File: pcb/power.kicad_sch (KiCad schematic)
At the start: 59 parts, among them J7 1S LiPo, Q1 Q_Dual_NMOS_S1G1S2G2D2D2D1D1, Q2 Q_Dual_NMOS_S1G1S2G2D2D2D1D1, U13 BQ25798, U14 TPS63060, U15 TPS61089

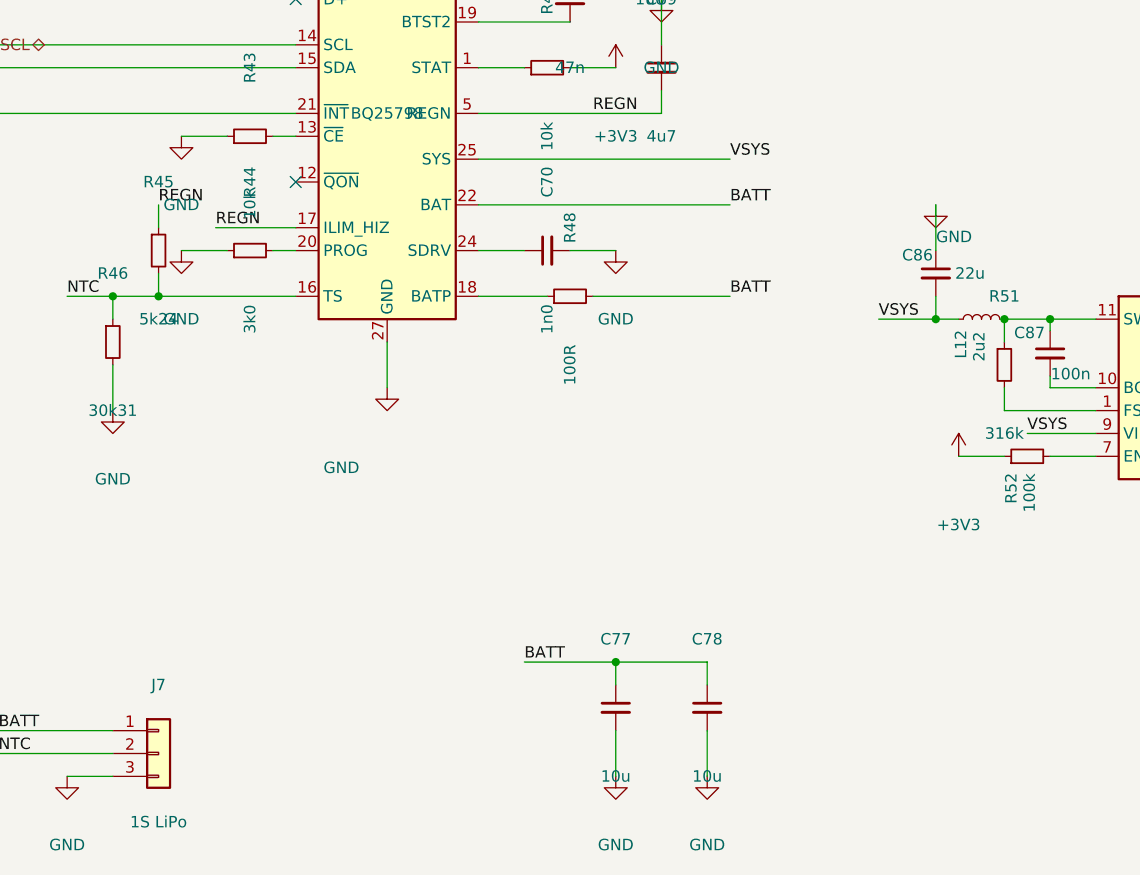
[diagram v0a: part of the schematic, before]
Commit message: give the battery a switch, so the board has an off
Patched into the power sheet the same way as the input pairs: named removals by coordinate, the new
work appended, nothing hand-placed moved.

The reason is in the schematic rather than in a datasheet. The 3.3V converter has its enable tied
straight to the system rail and the 5V converter's is pulled up to the 3.3V rail, so neither is
under firmware control, so for as long as the cell is connected the processor, the flash, the hub
and the port rail are all live and the deepest state firmware can reach is sleep. This switch is
the only thing on the board that disconnects the battery.

The argument is not that the charger leaks: its battery-only draw is 17uA, which on this cell is
measured in years. It is that everything else stays powered, and against that the charger's
shutdown state is 500nA. The size of that gap is the point. The figure on the other side of it is
an estimate of a sleeping-but-powered board and wants measuring rather than believing.

Wake is safe, which is the objection that would otherwise sink it: both low-power states wake
unconditionally on a charger being plugged in, and ship mode also by register or by the reset
input. No sequence strands the device.

The part is the one already in the design for the input pairs, both halves in parallel -- about
10 milliohms, so 35mV and 0.12W at the 3.5A peak and 18mV at the declared budget, and 30nC against
a 100nA charge pump at half duty is roughly 600ms to close, which is nothing for a power path.

Two consequences are easy to miss and both are taken. The capacitor that the driver pin wants when
no switch is fitted comes out, because against 100nA it would only add delay. And the battery sense
resistor stays on the cell side, so the charger can still see the battery while the switch is open
-- the same discipline that puts each input's detect pin outside its own pair. The drains face the
cell so the body diodes block pack-to-system when the switch is ope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
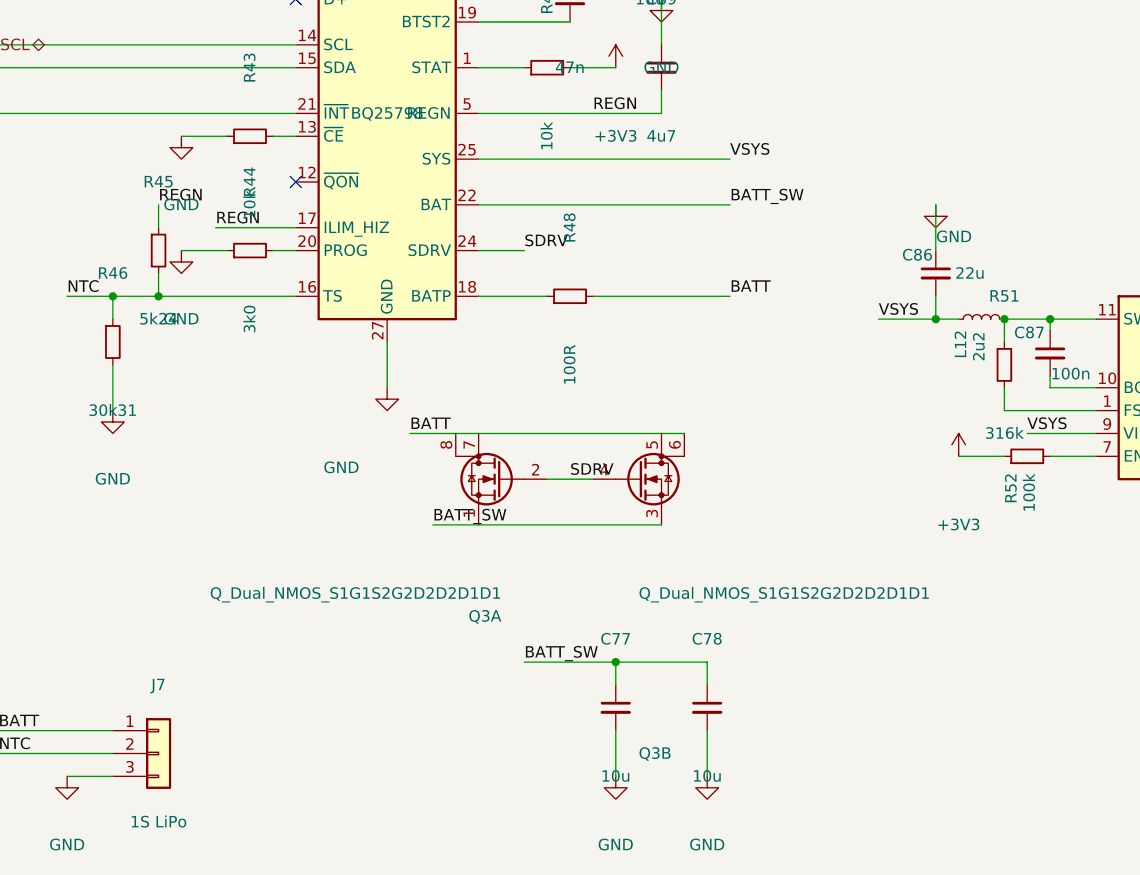
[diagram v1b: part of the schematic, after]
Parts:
- removed C70: 1n0, symbol Device:C_Small
- added Q3: Q_Dual_NMOS_S1G1S2G2D2D2D1D1, symbol Transistor_FET:Q_Dual_NMOS_S1G1S2G2D2D2D1D1
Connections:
- net BATT: now also Q3.5 (D), Q3.6 (D), Q3.7 (D), Q3.8 (D); no longer C77.1, C78.1, U13.22 (BAT), U13.23 (BAT)
- net SDRV: now reaches U13.24 (SDRV)
- net SDRV: now also Q3.2 (G), Q3.4 (G)
- new net BATT_SW: C77.1, C78.1, Q3.1 (S), Q3.3 (S), U13.22 (BAT), U13.23 (BAT)
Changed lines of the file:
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@@
 	(wire
 		(pts
-			(xy 198.12 149.86) (xy 203.2 149.86)
-		)
-		(stroke
-			(width 0)
-			(type solid)
-		)
-	)
-	(wire
-		(pts
 			(xy 109.22 82.55) (xy 118.11 82.55)
 		)
@@
 		)
 	)
-	(label "BATT"
+	(label "BATT_SW"
 		(at 193.04 195.58 0)
 		(effects
@@
 		)
 	)
-	(label "BATT"
+	(label "BATT_SW"
 		(at 215.9 144.78 0)
 		(effects
@@
 	)
 	(symbol
-		(lib_id "power:GND")
-		(at 203.2 149.86 0)
-		(unit 1)
-		(body_style 1)
-		(exclude_from_sim no)
-		(in_bom yes)
-		(on_board yes)
-		(in_pos_files yes)
-		(dnp no)
-		(property "Reference" "#PWR01"
-			(at 203.2 142.24 0)
-			(hide yes)
-			(show_name no)
-			(do_not_autoplace no)
-			(effects
-				(font
-					(size 1.27 1.27)
-				)
-			)
-		)
-		(property "Value" "GND"
-			(at 203.2 157.48 0)
-			(show_name no)
-			(do_not_autoplace no)
-			(effects
-				(font
-					(size 1.27 1.27)
-				)
-			)
-		)
-		(property "Footprint" ""
-			(at 203.2 149.86 0)
-			(show_name no)
-			(do_not_autoplace no)
-			(effects
-				(font
-					(size 1.27 1.27)
-				)
-			)
-		)
-		(property "Datasheet" ""
-			(at 203.2 149.86 0)
-			(show_name no)
-			(do_not_autoplace no)
-			(effects
-				(font
-					(size 1.27 1.27)
-				)
-			)
-		)
-		(property "Description" ""
-			(at 203.2 149.86 0)
-			(show_name no)
-			(do_not_autoplace no)
-			(effects
-				(font
-					(size 1.27 1.27)
-				)
-			)
-		)
-		(pin "1"
-		)
-		(instances
-			(project "crossfire"
-				(path "/4c5cdd13-4f54-43b0-affb-0ae4b9a4d279/3a0d800d-f868-47e5-a520-4703480651cc"
-					(reference "#PWR01")
-					(unit 1)
-				)
-			)
-		)
-	)
-	(symbol
 		(lib_id "Device:R_Small")
 		(at 246.38 162.56 0)
@@
 	)
 	(symbol
-		(lib_id "Device:C_Small")
-		(at 195.58 149.86 90)
-		(unit 1)
-		(body_style 1)
-		(exclude_from_sim no)
-		(in_bom yes)
-		(on_board yes)
-		(in_pos_files yes)
-		(dnp no)
-		(property "Reference" "C70"
-			(at 195.58 142.24 0)
-			(show_name no)
-			(do_not_autoplace no)
-			(effects
-				(font
-					(size 1.27 1.27)
-				)
-			)
-		)
-		(property "Value" "1n0"
-			(at 195.58 157.48 0)
-			(show_name no)
-			(do_not_autoplace no)
-			(effects
-				(font
-					(size 1.27 1.27)
-				)
-			)
-		)
-		(property "Footprint" ""
-			(at 195.58 149.86 0)
-			(show_name no)
-			(do_not_autoplace no)
-			(effects
-				(font
-					(size 1.27 1.27)
-				)
-			)
-		)
-		(property "Datasheet" ""
-			(at 195.58 149.86 0)
-			(show_name no)
-			(do_not_autoplace no)
-			(effects
-				(font
-					(size 1.27 1.27)
-				)
-			)
-		)
-		(property "Description" ""
-			(at 195.58 149.86 0)
-			(show_name no)
-			(do_not_autoplace no)
-			(effects
-				(font
-					(size 1.27 1.27)
-				)
-			)
-		)
-		(pin "1"
-		)
-		(pin "2"
-		)
-		(instances
-			(project "crossfire"
-				(path "/4c5cdd13-4f54-43b0-affb-0ae4b9a4d279/3a0d800d-f868-47e5-a520-4703480651cc"
-					(reference "C70")
-					(unit 1)
-				)
-			)
-		)
-	)
-	(symbol
 		(lib_id "power:+3V3")
 		(at 119.38 114.3 0)
@@
 		)
 	)
+	(symbol
+		(lib_id "Transistor_FET:Q_Dual_NMOS_S1G1S2G2D2D2D1D1")
+		(at 190.50 175.26 0)
+		(mirror y)
+		(unit 1)
+		(body_style 1)
+		(exclude_from_sim no)
+		(in_bom yes)
+		(on_board yes)
+		(in_pos_files yes)
+		(dnp no)
+		(property "Reference" "Q3"
+			(at 190.50 190.50 0)
+			(show_name no)
+			(do_not_autoplace no)
+			(effects
+				(font
+					(size 1.27 1.27)
+				)
+				(justify left)
+			)
+		)
+		(property "Value" "Q_Dual_NMOS_S1G1S2G2D2D2D1D1"
+			(at 190.50 187.96 0)
+			(show_name no)
+			(do_not_autoplace no)
+			(effects
+				(font
+					(size 1.27 1.27)
+				)
+				(justify left)
+			)
+		)
+		(property "Footprint" ""
+			(at 190.50 175.26 0)
+			(show_name no)
+			(do_not_autoplace no)
+			(effects
+				(font
+					(size 1.27 1.27)
+				)
+				(hide yes)
+			)
+		)
+		(property "Datasheet" ""
+			(at 190.50 175.26 0)
+			(show_name no)
+			(do_not_autoplace no)
+			(effects
+				(font
+					(size 1.27 1.27)
+				)
+				(hide yes)
+			)
+		)
+		(property "Description" ""
+			(at 190.50 175.26 0)
+			(show_name no)
+			(do_not_autoplace no)
+			(effects
+				(font
+					(size 1.27 1.27)
+				)
+				(hide yes)
+			)
+		)
+		(pin "1"
+		)
+		(pin "2"
+		)
+		(pin "7"
+		)
+		(pin "8"
+		)
+		(instances
+			(project "crossfire"
+				(path "/4c5cdd13-4f54-43b0-affb-0ae4b9a4d279/3a0d800d-f868-47e5-a520-4703480651cc"
+					(reference "Q3")
+					(unit 1)
+				)
+			)
+		)
+	)
+	(symbol
+		(lib_id "Transistor_FET:Q_Dual_NMOS_S1G1S2G2D2D2D1D1")
+		(at 205.74 175.26 0)
+		(unit 2)
+		(body_style 1)
+		(exclude_from_sim no)
+		(in_bom yes)
+		(on_board yes)
+		(in_pos_files yes)
+		(dnp no)
+		(property "Reference" "Q3"
+			(at 205.74 205.74 0)
+			(show_name no)
+			(do_not_autoplace no)
+			(effects
+				(font
+					(size 1.27 1.27)
+				)
+				(justify left)
+			)
+		)
+		(property "Value" "Q_Dual_NMOS_S1G1S2G2D2D2D1D1"
+			(at 205.74 187.96 0)
+			(show_name no)
+			(do_not_autoplace no)
+			(effects
+				(font
+					(size 1.27 1.27)
+				)
+				(justify left)
+			)
+		)
+		(property "Footprint" ""
+			(at 205.74 175.26 0)
+			(show_name no)
+			(do_not_autoplace no)
+			(effects
+				(font
+					(size 1.27 1.27)
+				)
+				(hide yes)
+			)
+		)
+		(property "Datasheet" ""
+			(at 205.74 175.26 0)
+			(show_name no)
+			(do_not_autoplace no)
+			(effects
+				(font
+					(size 1.27 1.27)
+				)
+				(hide yes)
+			)
+		)
+		(property "Description" ""
+			(at 205.74 175.26 0)
+			(show_name no)
+			(do_not_autoplace no)
+			(effects
+				(font
+					(size 1.27 1.27)
+				)
+				(hide yes)
+			)
+		)
+		(pin "3"
+		)
+		(pin "4"
+		)
+		(pin "5"
+		)
+		(pin "6"
+		)
+		(instances
+			(project "crossfire"
+				(path "/4c5cdd13-4f54-43b0-affb-0ae4b9a4d279/3a0d800d-f868-47e5-a520-4703480651cc"
+					(reference "Q3")
+					(unit 2)
+				)
+			)
+		)
+	)
+	(wire
+		(pts
+			(xy 195.58 175.26) (xy 200.66 175.26)
+		)
+		(stroke
+			(width 0)
+			(type default)
+		)
+	)
+	(label "SDRV"
+		(at 198.12 175.26 0)
+		(effects
+			(font
+				(size 1.27 1.27)
+			)
+			(justify left bottom)
+		)
+	)
+	(label "SDRV"
+		(at 193.04 149.86 0)
+		(effects
+			(font
+				(size 1.27 1.27)
+			)
+			(justify left bottom)
+		)
+	)
+	(wire
+		(pts
+			(xy 187.96 180.34) (xy 208.28 180.34)
+		)
+		(stroke
+			(width 0)
+			(type default)
+		)
+	)
+	(wire
+		(pts
+			(xy 182.88 180.34) (xy 187.96 180.34)
+		)
+		(stroke
+			(width 0)
+			(type default)
+		)
+	)
+	(label "BATT_SW"
+		(at 182.88 180.34 0)
+		(effects
+			(font
+				(size 1.27 1.27)
+			)
+			(justify left bottom)
+		)
+	)
+	(wire
+		(pts
+			(xy 185.42 170.18) (xy 187.96 170.18)
+		)
+		(stroke
+			(width 0)
+			(type default)
+		)
+	)
+	(wire
+		(pts
+			(xy 187.96 170.18) (xy 208.28 170.18)
+		)
+		(stroke
+			(width 0)
+			(type default)
+		)
+	)
+	(wire
+		(pts
+			(xy 208.28 170.18) (xy 210.82 170.18)
+		)
+		(stroke
+			(width 0)
+			(type default)
+		)
+	)
+	(wire
+		(pts
+			(xy 180.34 170.18) (xy 185.42 170.18)
+		)
+		(stroke
+			(width 0)
+			(type default)
+		)
+	)
+	(label "BATT"
+		(at 180.34 170.18 0)
+		(effects
+			(font
+				(size 1.27 1.27)
+			)
+			(justify left bottom)
+		)
+	)

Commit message: specify every capacitor: a rating and a dielectric, chosen from its net
A value on its own is not a specification. Each of the 62 capacitor symbols now carries a voltage
rating and a dielectric picked from the net it sits on -- at least twice the working voltage,
rounded to a standard rating, and never below what a socket the user can reach can present. Both
are hidden fields, so the drawing stays readable and a bill of materials can still be made from it.

Two of the choices are decisions rather than arithmetic.

The connector-side parts are rated for abuse at 50V, because nothing on the board protects them:
both input switches sit downstream of them, so the sink's own supply decoupling and the data
port's see whatever a hostile charger produces with no switch in between.

The charger's input bank is rated 25V on a condition, and the condition is firmware. The input
over-voltage trip defaults to 26V, which is above a 25V part, so rating the bank for its working
voltage is only safe if that trip comes down. The part offers 7V, 12V, 22V and 26V and 12V is the
right one here: the sink never asks for more than 9V, so 12V clears the profile with room and
bounds what the bank can ever see. A board decision that creates a firmware requirement is exactly
the sort that gets lost, so it is recorded on both sides.

What is left open is what the banks are worth once fitted. The charger specifies them as counts of
10uF parts, which only means something if each part is still worth 10uF where it sits, and a
ceramic at 9V is not. The rating and the dielectric are settled; the package is not, and the
package is what decides how much survives. The footprint step has to read each chosen part's bias
curve and add parts if the effective value falls short rather than assume the count was the point.
That is the one piece of this specification that can still change the part count.

Rules check unchanged, and the schematic check is clean.

Co-Authored-By: Claude Opus 5 (1M context) <norepl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
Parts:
- C60, C61, C62, C63, C64, C65, C66, C89, C90, C91: Dielectric (none) -> X7R; Voltage (none) -> 25V
- C67, C68, C69, C71, C72, C73, C74, C75, C76, C77, C78, C79, C80, C81, C82, C83, C85, C86, C87, C88: Dielectric (none) -> X7R; Voltage (none) -> 16V
- C84: Dielectric (none) -> C0G; Voltage (none) -> 50V
- C92: Dielectric (none) -> C0G; Voltage (none) -> 16V

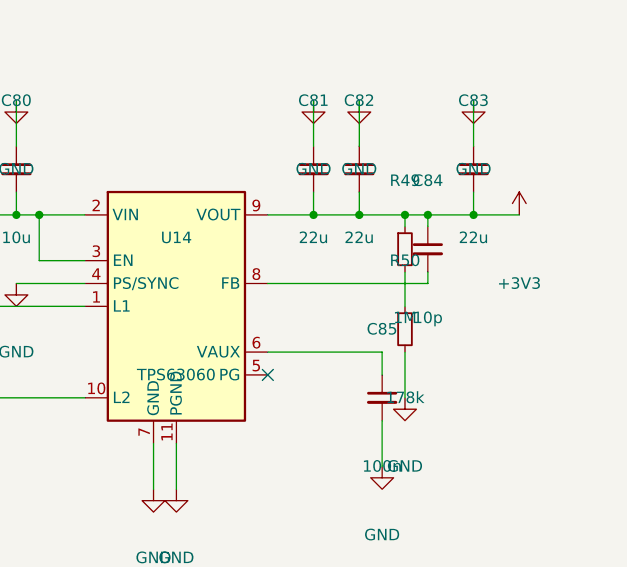
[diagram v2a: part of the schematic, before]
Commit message: connect the 3.3V feedback divider, which was crossing its own feedback line
The divider that sets the 3.3V rail was not connected to the pin it sets. The values are right --
1M over 178k against a 500mV reference gives 3.3V -- and the midpoint wire crossed the feedback
line with no junction at the crossing, one grid step from joining it, which draws exactly like a
connection. That rail feeds the processor, the flash, the hub and the radio, and with no feedback
the converter has nothing telling it when to stop. It would not have survived first power-up.

The rules check says nothing whatever about it. That was measured rather than assumed: putting the
fault back into a copy moved no violation at all. Nor would the checks added yesterday have found
it, since the midpoint is a net with two nodes rather than a stub, and nothing is bridged.

So the checker gains two questions. Which wires end part-way along another wire with no junction
dot -- the editor adds one when you draw it that way, a file edited by other means does not get
one. And which nets reach nothing but two-terminal passives, which is the shape of a divider whose
output never arrived. The second is reported rather than failed, because a series compensation
network has the same shape honestly; on this board it returns two lines and the difference between
them is plain. Both were proven by removing a junction of each kind from a copy and watching them
fire.

Co-Authored-By: Claude Opus 5 (1M context) <noreply@anthropic.com>
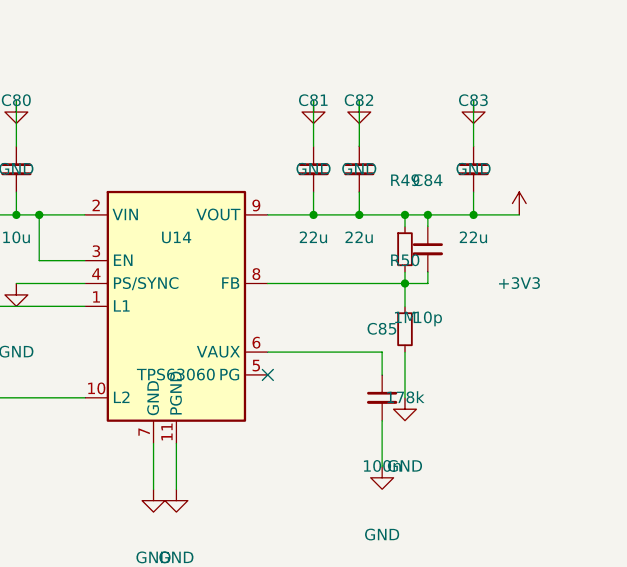
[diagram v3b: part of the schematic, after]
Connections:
- net at R49.2, R50.1: now also C84.2, U14.8 (FB)
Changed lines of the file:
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@@
 		)
 	)
+	(junction
+		(at 292.10 99.06)
+		(diameter 0)
+		(color 0 0 0 0)
+	)
 )
